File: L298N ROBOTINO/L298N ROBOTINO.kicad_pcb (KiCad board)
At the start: 2 copper layers, 39 parts, among them U2 L298N, U4 ESP32-DevKitC, U5 NRF24L01_Breakout, U6 L298N

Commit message: Da noi day xong
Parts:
- moved C3 87.0 mm to (58.3, 60.0), turned to 180 degrees
- moved C9 80.0 mm to (58.1, 66.6), turned to 180 degrees
- moved C8 71.8 mm to (58.0, 72.6), turned to 180 degrees
- moved C7 66.1 mm to (56.0, 129.0), turned to 0 degrees
- moved C1 63.1 mm to (56.0, 135.0), turned to 0 degrees
- moved C4 62.5 mm to (58.0, 79.6), turned to 180 degrees
- moved C2 62.1 mm to (56.0, 118.0)
- moved C6 58.1 mm to (56.0, 123.6), turned to 0 degrees
- moved U3 45.4 mm to (72.0, 76.0), turned to 90 degrees
- moved C10 36.6 mm to (90.5, 110.0)
- moved C11 36.6 mm to (90.5, 106.0)
- moved U1 31.3 mm to (72.0, 121.0), turned to -90 degrees
- moved D10 31.3 mm to (92.9, 161.1)
- moved D11 31.3 mm to (107.0, 161.1)
- moved D12 31.3 mm to (92.9, 166.1)
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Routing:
- net GND: track 0.00 -> 377.6 mm, vias 0 -> 4
- net +8V: track 0.00 -> 235.9 mm, vias 0 -> 3
- net +5V: track 0.00 -> 163.4 mm, vias 0 -> 3
- net EnA: track 0.00 -> 128.2 mm, vias 0 -> 6
- net IN3: track 0.00 -> 119.1 mm, vias 0 -> 3
- net IN4: track 0.00 -> 119.0 mm
- net IN2: track 0.00 -> 113.1 mm, vias 0 -> 3
- net IN1: track 0.00 -> 110.7 mm, vias 0 -> 4
- net EnB: track 0.00 -> 110.2 mm, vias 0 -> 2
- net +3.3V: track 0.00 -> 89.0 mm, vias 0 -> 1
- net Net-(D6-A): track 0.00 -> 81.5 mm, vias 0 -> 1
- net Net-(D8-A): track 0.00 -> 75.2 mm
- net Net-(D14-A): track 0.00 -> 67.9 mm, vias 0 -> 1
- net Net-(D4-A): track 0.00 -> 66.8 mm, vias 0 -> 3
- net Net-(D2-A): track 0.00 -> 66.3 mm, vias 0 -> 1
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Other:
- board outline added: 113.5 x 159 mm

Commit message: New PCB ver 2 Edit
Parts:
- moved D10 127.9 mm to (171.8, 60.4), turned to 180 degrees
- moved D12 126.5 mm to (171.8, 67.2), turned to 180 degrees
- moved D14 125.1 mm to (171.8, 74.0), turned to 180 degrees
- moved D16 123.8 mm to (171.9, 80.8), turned to 180 degrees
- moved MotorA_F2 123.3 mm to (158.1, 64.2)
- moved D11 111.6 mm to (161.6, 63.8)
- moved C13 111.5 mm to (143.9, 56.9), turned to 180 degrees
- moved D13 110.0 mm to (161.6, 70.6)
- moved D15 108.5 mm to (161.6, 77.4)
- moved D17 106.8 mm to (161.6, 84.4)
- moved C9 91.5 mm to (108.3, 143.2), turned to 0 degrees
- moved U6 88.0 mm to (138.7, 63.5), turned to -90 degrees
- moved C8 84.0 mm to (108.3, 140.0), turned to 0 degrees
- moved C3 83.6 mm to (108.3, 127.0), turned to 0 degrees
- moved MotorB_F2 79.8 mm to (158.0, 78.1)
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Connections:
- U4 pad 26: Net-(U4-ADC2_CH0/GPIO4) -> unconnected-(U4-ADC2_CH0/GPIO4-Pad26)
- U4 pad 27: unconnected-(U4-GPIO16-Pad27) -> CSN
- U4 pad 28: unconnected-(U4-GPIO17-Pad28) -> Net-(U4-GPIO17)
- U4 pad 29: CSN -> unconnected-(U4-GPIO5-Pad29)
- U5 pad 3: Net-(U4-ADC2_CH0/GPIO4) -> Net-(U4-GPIO17)
- U5 pad 8: unconnected-(U5-IRQ-Pad8) -> Net-(U4-GPIO17)
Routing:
- net Net-(D6-A): track 81.5 -> 21.5 mm, vias 1 -> 0
- net Net-(D8-A): track 75.2 -> 28.8 mm
- net Net-(D4-A): track 66.8 -> 21.0 mm, vias 3 -> 0
- net EnA: track 128.2 -> 84.1 mm, vias 6 -> 1
- net Net-(D16-A): track 66.0 -> 21.9 mm
- net Net-(D2-A): track 66.3 -> 26.6 mm, vias 1 -> 2
- net +3.3V: track 89.0 -> 50.0 mm, vias 1 -> 0
- net EnB: track 110.2 -> 77.9 mm
- net Net-(D12-A): track 59.0 -> 26.8 mm
- net IN4: track 119.0 -> 88.2 mm
- net Net-(D14-A): track 67.9 -> 37.2 mm, vias 1 -> 0
- net IN3: track 119.1 -> 88.8 mm, vias 3 -> 1
- net +8V: track 235.9 -> 261.7 mm, vias 3 -> 1
- net IN2: track 113.1 -> 88.6 mm, vias 3 -> 1
- net Net-(U4-ADC2_CH0/GPIO4): track 24.0 -> 0.00 mm, vias 1 -> 0
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- added copper zone on F.Cu, net GND
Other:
- board size 113.5 x 159 mm -> 129.1 x 97.8 mm

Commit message: PCB CHO BOARD HAN
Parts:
- moved MotorA_F2 55.1 mm to (210.8, 48.3)
- moved MotorB_F2 53.7 mm to (210.8, 68.6)
- moved D9 47.2 mm to (109.2, 41.4)
- moved D8 46.6 mm to (109.2, 45.7), turned to 180 degrees
- moved D11 44.4 mm to (203.2, 48.3), turned to 180 degrees
- moved D13 44.1 mm to (203.2, 55.9), turned to 180 degrees
- moved D15 43.8 mm to (203.2, 63.5), turned to 180 degrees
- moved D17 43.6 mm to (203.2, 71.1), turned to 180 degrees
- moved D6 36.7 mm to (109.2, 54.2), turned to 180 degrees
- moved D10 35.2 mm to (203.2, 44.5)
- moved D12 34.9 mm to (203.2, 52.1)
- moved D14 34.5 mm to (203.2, 59.7)
- moved D7 34.2 mm to (109.2, 49.9)
- moved D16 34.1 mm to (203.2, 67.3)
- moved U2 32.9 mm to (138.4, 67.3), turned to 90 degrees
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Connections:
- U2 pad 11: EnB -> EnB_L
- U2 pad 6: EnA -> EnA_L
- U4 pad 28: Net-(U4-GPIO17) -> CE
- U4 pad 37: MOSI -> unconnected-(U4-GPIO23-Pad37)
- U4 pad 5: unconnected-(U4-VDET_1/GPIO34/ADC1_CH6-Pad5) -> EnA_L
- U4 pad 6: unconnected-(U4-VDET_2/GPIO35/ADC1_CH7-Pad6) -> EnB_L
- U4 pad 7: EnB -> EnB_R
- U4 pad 8: EnA -> EnA_R
- U5 pad 3: Net-(U4-GPIO17) -> CE
- U5 pad 6: MOSI -> unconnected-(U5-MOSI-Pad6)
- U5 pad 8: Net-(U4-GPIO17) -> unconnected-(U5-IRQ-Pad8)
- U6 pad 11: EnB -> EnB_R
- U6 pad 6: EnA -> EnA_R
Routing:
- net GND: track 364.0 -> 484.0 mm, vias 0 -> 8
- net EnA: track 84.1 -> 0.00 mm, vias 1 -> 0
- net EnB_R: track 0.00 -> 80.0 mm, vias 0 -> 2
- net EnB: track 77.9 -> 0.00 mm, vias 2 -> 0
- net EnA_R: track 0.00 -> 71.1 mm, vias 0 -> 4
- net EnA_L: track 0.00 -> 71.1 mm, vias 0 -> 3
- net EnB_L: track 0.00 -> 54.6 mm, vias 0 -> 2
- net Net-(D10-A): track 23.3 -> 75.2 mm, vias 0 -> 1
- net Net-(D16-A): track 21.9 -> 62.5 mm, vias 0 -> 1
- net +8V: track 261.7 -> 301.1 mm, vias 1 -> 5
- net Net-(D4-A): track 21.0 -> 57.2 mm, vias 0 -> 2
- net MOSI: track 33.2 -> 0.00 mm
- net Net-(D12-A): track 26.8 -> 58.7 mm, vias 0 -> 1
- net IN4: track 88.2 -> 119.4 mm, vias 0 -> 4
- net +5V: track 147.0 -> 177.9 mm, vias 0 -> 6
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- added copper zone on F.Cu, net (none)
- removed copper zone on F.Cu, net GND
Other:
- board size 129.1 x 97.8 mm -> 140 x 105 mm

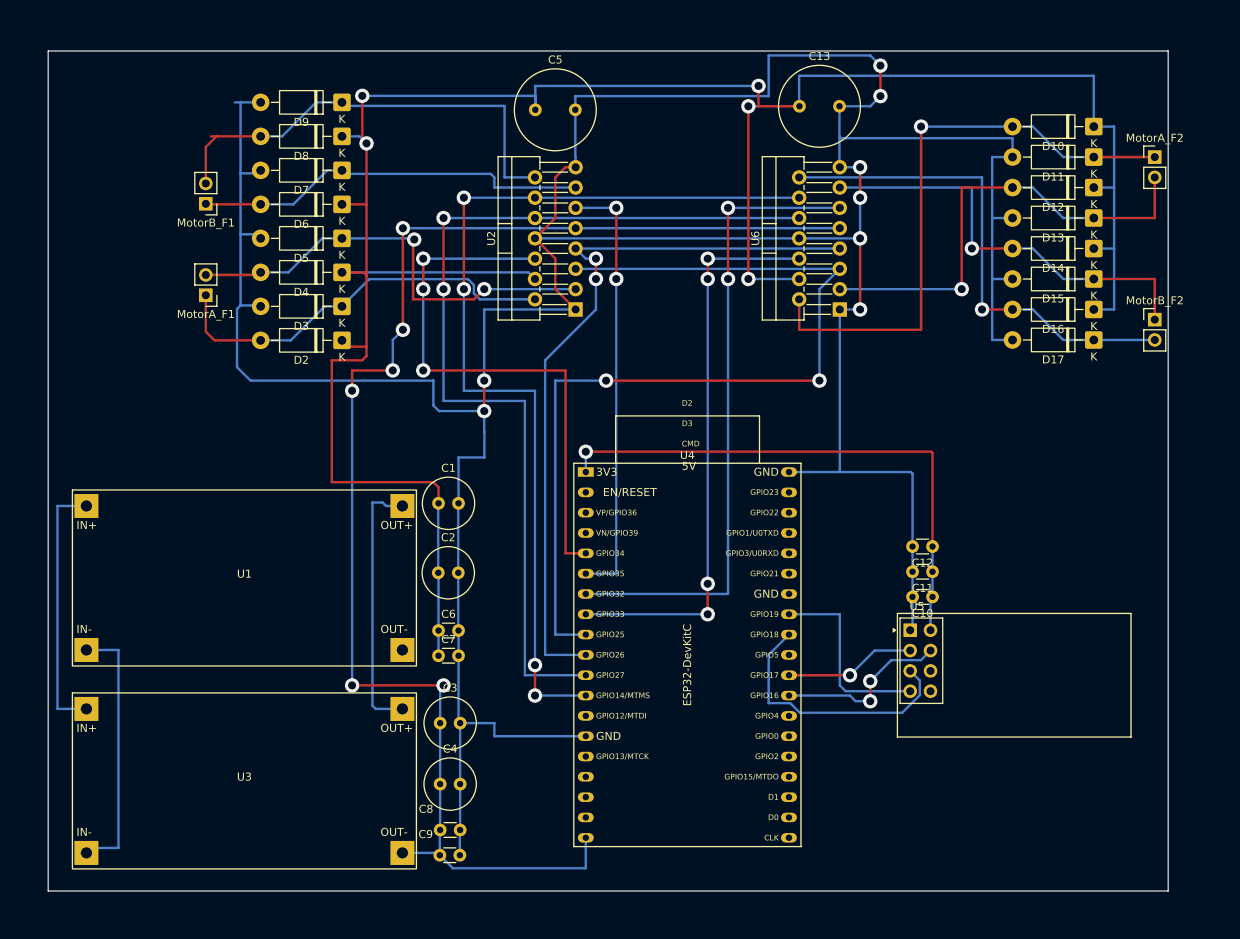
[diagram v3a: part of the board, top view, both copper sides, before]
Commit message: Finished L298N PCB, added a 74hc14 to reduce gpios required, changed PCB to 4 layers to add extra wiring, fixed footprints, fixed pin labels
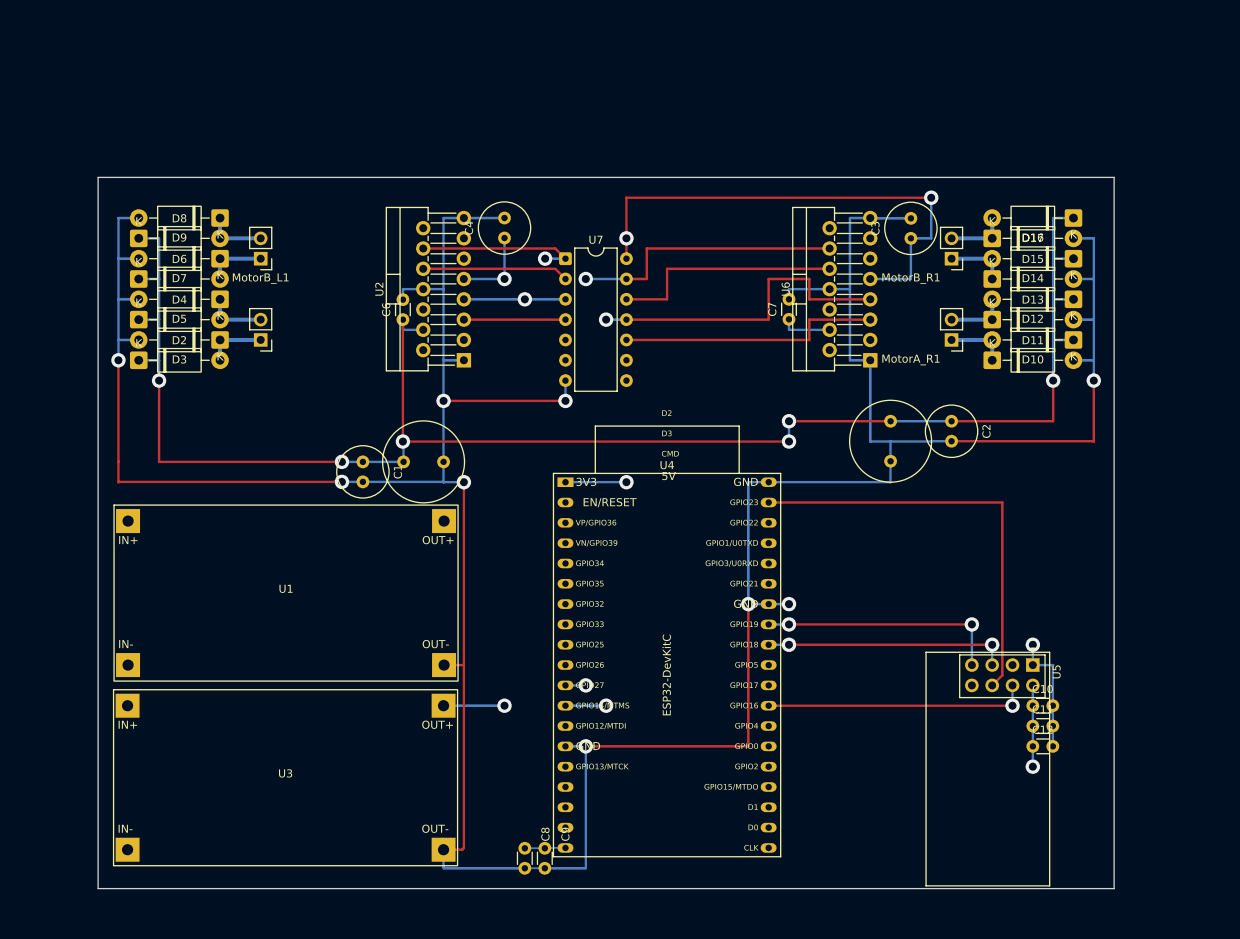
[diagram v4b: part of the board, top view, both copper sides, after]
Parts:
- removed MotorA_F1, MotorA_F2, MotorB_F1, MotorB_F2: Conn_01x02, Connector_PinHeader_2.54mm:PinHeader_1x02_P2.54mm_Vertical
- added MotorA_L1: Conn_01x02, Connector_PinHeader_2.54mm:PinHeader_1x02_P2.54mm_Vertical, F.Cu at (99.1, 71.1)
- added MotorA_R1: Conn_01x02, Connector_PinHeader_2.54mm:PinHeader_1x02_P2.54mm_Vertical, F.Cu at (185.4, 71.1)
- added MotorB_L1: Conn_01x02, Connector_PinHeader_2.54mm:PinHeader_1x02_P2.54mm_Vertical, F.Cu at (99.1, 61.0)
- added MotorB_R1: Conn_01x02, Connector_PinHeader_2.54mm:PinHeader_1x02_P2.54mm_Vertical, F.Cu at (185.4, 61.0)
- added U7: 74HC14, Package_DIP:DIP-14_W7.62mm, F.Cu at (137.2, 61.0)
- U1, U3: footprint ROBOTINO:LM2596S_Module -> LM2596S:LM2596S_Module
- moved C3 84.5 mm to (180.3, 58.4), turned to 90 degrees
- moved C4 68.7 mm to (129.5, 58.4), turned to 90 degrees
- moved C2 66.9 mm to (185.4, 81.3), turned to -90 degrees
- moved C7 60.7 mm to (165.1, 68.5), turned to 90 degrees
- moved C5 47.0 mm to (116.9, 86.4)
- moved C13 41.0 mm to (177.8, 81.3), turned to -90 degrees
- moved C6 39.1 mm to (116.8, 68.6), turned to 90 degrees
- moved D8 28.4 mm to (83.8, 58.4), turned to 0 degrees
- moved D11 28.4 mm to (190.5, 73.7), turned to 0 degrees
- moved C12 28.0 mm to (195.6, 121.9), turned to 0 degrees
- moved D6 27.1 mm to (83.8, 63.5), turned to 0 degrees
- moved D10 26.8 mm to (200.7, 71.1)
- moved D4 26.1 mm to (83.8, 68.6), turned to 0 degrees
- moved D2 25.5 mm to (83.8, 73.7), turned to 0 degrees
- moved C11 23.0 mm to (195.6, 119.4), turned to 0 degrees
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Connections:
- U2 pad 10: IN3 -> IN3_L
- U2 pad 12: IN4 -> IN4_L
- U2 pad 5: IN1 -> IN1_L
- U2 pad 7: IN2 -> IN2_L
- U4 pad 10: IN2 -> EnA_L
- U4 pad 11: IN3 -> IN4_R
- U4 pad 12: IN4 -> IN2_R
- U4 pad 33: unconnected-(U4-GPIO21-Pad33) -> EnA_R
- U4 pad 36: unconnected-(U4-GPIO22-Pad36) -> EnB_R
- U4 pad 37: unconnected-(U4-GPIO23-Pad37) -> MOSI
- U4 pad 5: EnA_L -> unconnected-(U4-VDET_1/GPIO34/ADC1_CH6-Pad5)
- U4 pad 6: EnB_L -> unconnected-(U4-VDET_2/GPIO35/ADC1_CH7-Pad6)
- U4 pad 7: EnB_R -> IN4_L
- U4 pad 8: EnA_R -> EnB_L
- U4 pad 9: IN1 -> IN2_L
- U5 pad 6: unconnected-(U5-MOSI-Pad6) -> MOSI
- U6 pad 10: IN3 -> IN3_R
- U6 pad 12: IN4 -> IN4_R
- U6 pad 5: IN1 -> IN1_R
- U6 pad 7: IN2 -> IN2_R
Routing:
- net IN4: track 119.4 -> 0.00 mm, vias 4 -> 0
- net IN3: track 119.4 -> 0.00 mm, vias 2 -> 0
- net IN1: track 116.6 -> 0.00 mm, vias 2 -> 0
- net IN2_R: track 0.00 -> 94.0 mm, vias 0 -> 2
- net IN2: track 93.3 -> 0.00 mm, vias 2 -> 0
- net IN4_R: track 0.00 -> 87.6 mm, vias 0 -> 2
- net IN4_L: track 0.00 -> 66.6 mm, vias 0 -> 1
- net +3.3V: track 68.2 -> 129.5 mm, vias 1 -> 2
- net IN2_L: track 0.00 -> 61.0 mm, vias 0 -> 1
- net +8V: track 301.1 -> 241.6 mm, vias 5 -> 6
- net MOSI: track 0.00 -> 52.6 mm
- net Net-(D10-A): track 75.2 -> 23.4 mm, vias 1 -> 0
- net Net-(D12-A): track 58.7 -> 18.8 mm, vias 1 -> 0
- net Net-(D16-A): track 62.5 -> 23.4 mm, vias 1 -> 0
- net EnB_R: track 80.0 -> 45.7 mm, vias 2 -> 0
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- added copper zone on F.Cu, net IN1_R
- removed copper zone on F.Cu, net (none)
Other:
- board size 140 x 105 mm -> 127 x 88.9 mm
- copper layers 2 -> 4
- board text added: "127mm"
- board text added: "3500 mils"
- board text added: "5000 mils"
- board text added: "88.9mm"
